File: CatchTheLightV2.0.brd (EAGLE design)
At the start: 45 x 100 mm, 44 parts, among them J1 TC2030-IDC-NL, U1 ATMEGA328PB-ANR

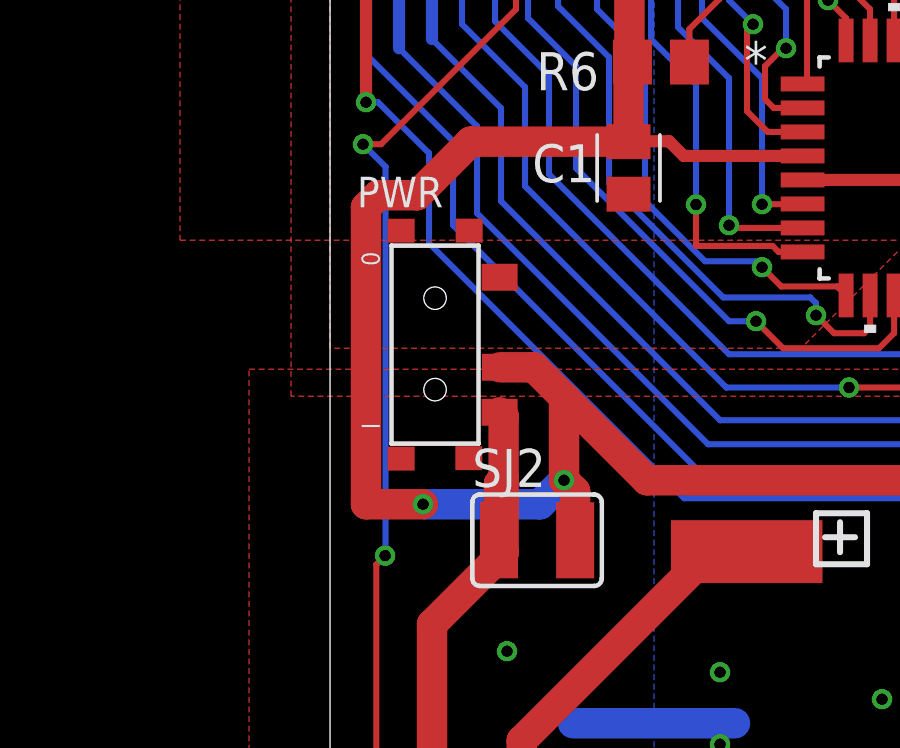
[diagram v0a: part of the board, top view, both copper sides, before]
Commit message: Moved switch in from edge of board for more clearance
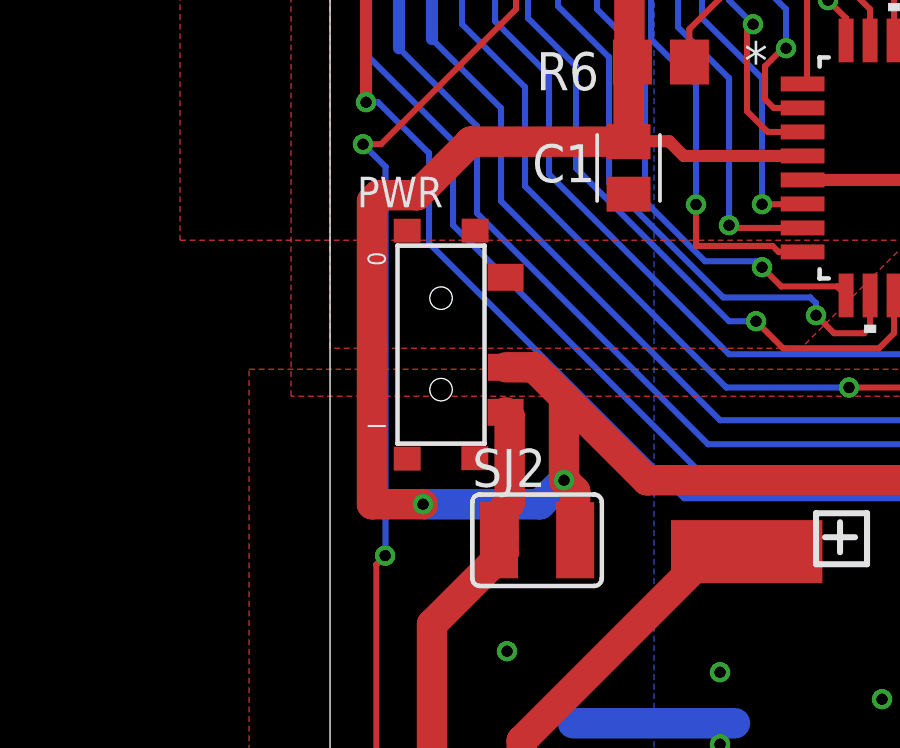
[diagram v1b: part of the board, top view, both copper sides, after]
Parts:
- moved PB1 0.20 mm to (5.25, 52.5)
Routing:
- net PROTECTED_VBAT: track 38.7 -> 36.9 mm
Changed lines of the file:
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@@
 <attribute name="POPULARITY" value="68" x="-30.9625" y="16.5375" size="1.778" layer="27" rot="R270" display="off"/>
 </element>
-<element name="PB1" library="ECE_388_CustomParts_V1.1" package="SK-3296S-01-L1" value="SK-3296S-01-L1" x="5.05" y="52.52" smashed="yes" rot="R270"/>
+<element name="PB1" library="ECE_388_CustomParts_V1.1" package="SK-3296S-01-L1" value="SK-3296S-01-L1" x="5.25" y="52.52" smashed="yes" rot="R270"/>
 <element name="PB2" library="ECE_388_CustomParts_V1.1" package="TS-1102S-C-A-B" value="PB2" x="2.4" y="12.46" smashed="yes"/>
 <element name="R1" library="rcl" library_urn="urn:adsk.eagle:library:334" package="R0805" package3d_urn="urn:adsk.eagle:package:23553/2" value="330" x="22.48" y="76.49" smashed="yes" rot="R270">
@@
 <contactref element="PB1" pad="P3"/>
 <contactref element="SJ1" pad="2"/>
-<wire x1="5.7862" y1="42.1862" x2="5.7862" y2="44.6404125" width="1.016" layer="1"/>
+<wire x1="5.7862" y1="42.1862" x2="5.7862" y2="42.7562" width="1.016" layer="1"/>
 <wire x1="3.4" y1="39.8" x2="5.7862" y2="42.1862" width="1.016" layer="1"/>
 <contactref element="SJ2" pad="1"/>
-<wire x1="5.63" y1="42.6" x2="5.63" y2="44.4842125" width="1.016" layer="1"/>
-<wire x1="5.63" y1="44.4842125" x2="5.7862" y2="44.6404125" width="1.016" layer="1"/>
-<wire x1="5.7862" y1="46.7313" x2="5.7862" y2="44.6404125" width="1.016" layer="1"/>
-<wire x1="5.7862" y1="46.7313" x2="5.6525" y2="46.865" width="1.016" layer="1"/>
+<wire x1="5.7862" y1="43.6404125" x2="5.7862" y2="42.7562" width="1.016" layer="1"/>
+<wire x1="5.63" y1="42.6" x2="5.7862" y2="42.7562" width="1.016" layer="1"/>
+<wire x1="5.7862" y1="43.6404125" x2="5.9862" y2="43.8404125" width="1.016" layer="1"/>
+<wire x1="5.8525" y1="46.865" x2="5.9862" y2="46.7313" width="1.016" layer="1"/>
+<wire x1="5.9862" y1="46.7313" x2="5.9862" y2="43.8404125" width="1.016" layer="1"/>
 <contactref element="T1" pad="2"/>
 <wire x1="3.4" y1="22.27" x2="4.2" y2="21.47" width="1.016" layer="1"/>
@@
 <wire x1="2.9" y1="54.1" x2="4.6854" y2="55.8854" width="1.016" layer="1"/>
 <wire x1="2.9" y1="54.1" x2="1.6" y2="54.1" width="1.016" layer="1"/>
-<wire x1="1.6" y1="54.1" x2="1.2" y2="53.7" width="1.016" layer="1"/>
-<wire x1="1.2" y1="53.7" x2="1.2" y2="43.8" width="1.016" layer="1"/>
-<wire x1="1.2" y1="43.8" x2="3.1" y2="43.8" width="1.016" layer="1"/>
+<wire x1="1.6" y1="54.1" x2="1.4" y2="53.9" width="1.016" layer="1"/>
+<wire x1="1.4" y1="53.9" x2="1.4" y2="43.8" width="1.016" layer="1"/>
+<wire x1="1.4" y1="43.8" x2="3.1" y2="43.8" width="1.016" layer="1"/>
 <via x="3.1" y="43.8" extent="1-16" drill="0.381"/>
 <wire x1="7.8" y1="44.6" x2="7" y2="43.8" width="1.016" layer="16"/>
@@
 <wire x1="24.2525" y1="53.01" x2="26.69" y2="53.01" width="0.4064" layer="1"/>
 <wire x1="22.48" y1="75.54" x2="21.94" y2="75" width="1.016" layer="1"/>
-<wire x1="5.665" y1="48.365" x2="6.7975" y2="48.365" width="1.016" layer="1"/>
+<wire x1="5.865" y1="48.365" x2="6.7975" y2="48.365" width="1.016" layer="1"/>
 <wire x1="28.8" y1="53.3421" x2="28.2579" y2="53.3421" width="0.4064" layer="1"/>
 <wire x1="28.4" y1="51.8" x2="29.4" y2="51.8" width="0.4064" layer="16"/>
